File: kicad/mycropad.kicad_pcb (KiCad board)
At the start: 2 copper layers, 116.2 x 64.8 mm, 25 parts, among them SW1 SW_Push, SW2 SW_Push, SW3 SW_Push, SW4 SW_Push, SW5 SW_Push, SW6 SW_Push, SW7 SW_Push, SW8 SW_Push, U1 Pico, U2 SN74AHCT125N

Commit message: New reverse mount led. Let's hope it works...
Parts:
- added C1: 10uF, Capacitor_SMD:C_1206_3216Metric_Pad1.33x1.80mm_HandSolder, B.Cu at (116.8, 67.7)
- added C2: 10uF, Capacitor_SMD:C_1206_3216Metric_Pad1.33x1.80mm_HandSolder, B.Cu at (135.9, 67.7)
- added C3: 10uF, Capacitor_SMD:C_1206_3216Metric_Pad1.33x1.80mm_HandSolder, B.Cu at (116.8, 86.7)
- added C4: 10uF, Capacitor_SMD:C_1206_3216Metric_Pad1.33x1.80mm_HandSolder, B.Cu at (135.9, 86.7)
- added C5: 10uF, Capacitor_SMD:C_1206_3216Metric_Pad1.33x1.80mm_HandSolder, B.Cu at (116.8, 105.8)
- added C6: 10uF, Capacitor_SMD:C_1206_3216Metric_Pad1.33x1.80mm_HandSolder, B.Cu at (135.9, 105.8)
- added C7: 10uF, Capacitor_SMD:C_1206_3216Metric_Pad1.33x1.80mm_HandSolder, B.Cu at (154.9, 105.8)
- added C8: 10uF, Capacitor_SMD:C_1206_3216Metric_Pad1.33x1.80mm_HandSolder, B.Cu at (174.0, 105.8)
- D1, D2, D3, D4, D5, D6, D7, D8: value COM-12999 -> SK6812MINI-E; footprint LED_THT:LED_D5.0mm-4_RGB -> mycropad:LED_SK6812MINI-E_REV02_PLCC4_3.5x3.5mm_P1.75mm; moved to B.Cu
- moved D1 2.54 mm to (116.9, 70.9)
- moved D3 2.52 mm to (116.8, 89.9)
- moved D5 2.52 mm to (116.8, 109.0)
- moved D7 2.52 mm to (154.9, 109.0)
- moved D8 2.52 mm to (174.0, 109.0)
- moved D2 2.52 mm to (135.9, 70.9)
- moved D4 2.52 mm to (135.9, 89.9)
- moved D6 2.52 mm to (135.9, 109.0)
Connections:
- D1 pad 1: Net-(D1-Pad1) -> +5V
- D1 pad 2: +5V -> Net-(D1-Pad2)
- D2 pad 1: Net-(D1-Pad4) -> +5V
- D2 pad 2: +5V -> Net-(D2-Pad2)
- D2 pad 4: Net-(D2-Pad4) -> Net-(D1-Pad2)
- D3 pad 1: Net-(D2-Pad4) -> +5V
- D3 pad 2: +5V -> Net-(D3-Pad2)
- D3 pad 4: Net-(D3-Pad4) -> Net-(D2-Pad2)
- D4 pad 1: Net-(D3-Pad4) -> +5V
- D4 pad 2: +5V -> Net-(D4-Pad2)
- D4 pad 4: Net-(D4-Pad4) -> Net-(D3-Pad2)
- D5 pad 1: Net-(D4-Pad4) -> +5V
- D5 pad 2: +5V -> Net-(D5-Pad2)
- D5 pad 4: Net-(D5-Pad4) -> Net-(D4-Pad2)
- D6 pad 1: Net-(D5-Pad4) -> +5V
- D6 pad 2: +5V -> Net-(D6-Pad2)
- D6 pad 4: Net-(D6-Pad4) -> Net-(D5-Pad2)
- D7 pad 1: Net-(D6-Pad4) -> +5V
- D7 pad 2: +5V -> Net-(D7-Pad2)
- D7 pad 4: Net-(D7-Pad4) -> Net-(D6-Pad2)
- D8 pad 1: Net-(D7-Pad4) -> +5V
- D8 pad 2: +5V -> Net-(D8-Pad2)
- D8 pad 4: Net-(D8-Pad4) -> Net-(D7-Pad2)
- R1 pad 1: Net-(D1-Pad1) -> Net-(D1-Pad4)
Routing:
- net GND: track 418.7 -> 493.5 mm
- net Net-(D2-Pad2): track 0.00 -> 50.6 mm, vias 0 -> 2
- net Net-(D4-Pad2): track 0.00 -> 50.4 mm, vias 0 -> 2
- net Net-(D4-Pad4): track 42.5 -> 0.00 mm
- net Net-(D2-Pad4): track 42.5 -> 0.00 mm
- net Net-(D1-Pad1): track 39.8 -> 0.00 mm
- net Net-(D1-Pad4): track 15.2 -> 48.4 mm, vias 0 -> 1
- net +5V: track 227.2 -> 247.9 mm
- net Net-(D7-Pad4): track 15.2 -> 0.00 mm
- net Net-(D6-Pad4): track 15.2 -> 0.00 mm
- net Net-(D5-Pad4): track 15.2 -> 0.00 mm
- net Net-(D3-Pad4): track 15.2 -> 0.00 mm
- net Net-(D5-Pad2): track 0.00 -> 13.8 mm, vias 0 -> 2
- net Net-(D3-Pad2): track 0.00 -> 13.8 mm, vias 0 -> 2
- net Net-(D1-Pad2): track 0.00 -> 13.8 mm, vias 0 -> 2
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
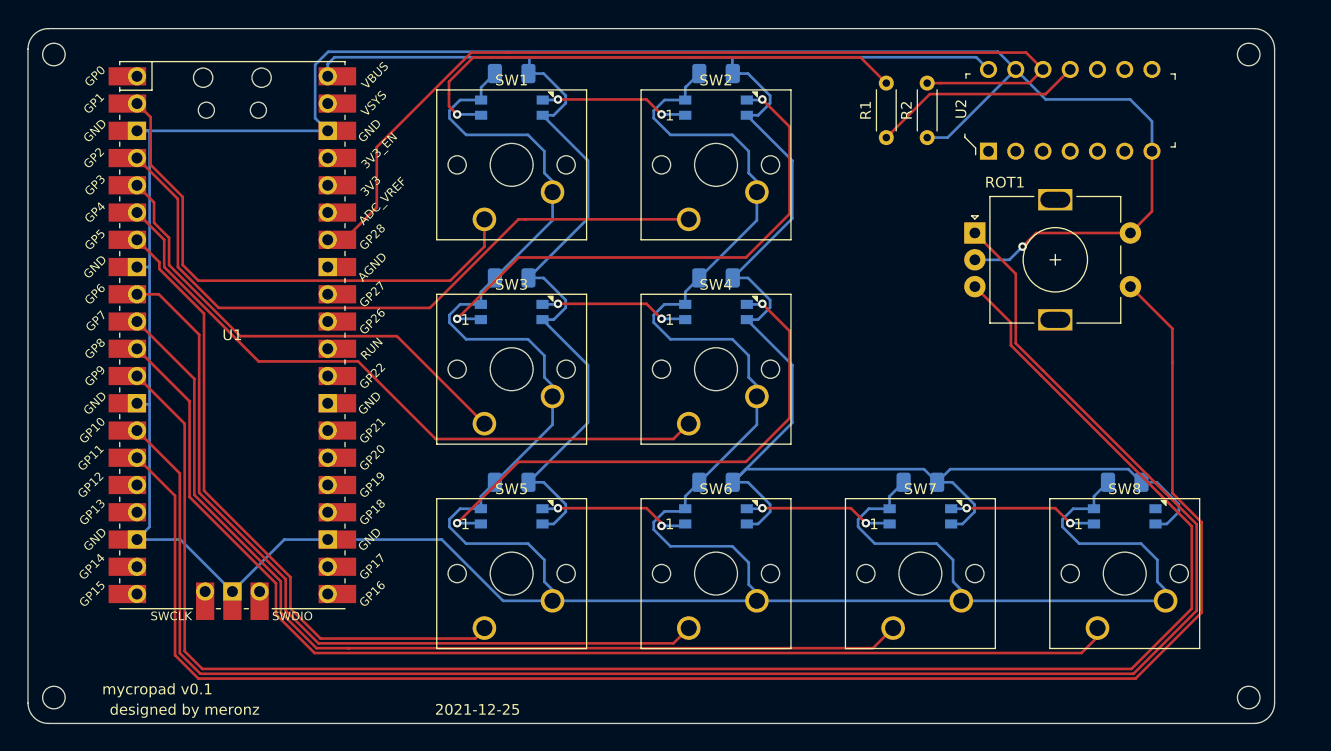
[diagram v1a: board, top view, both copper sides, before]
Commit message: Updated footprints for SK6812 MINI-E.
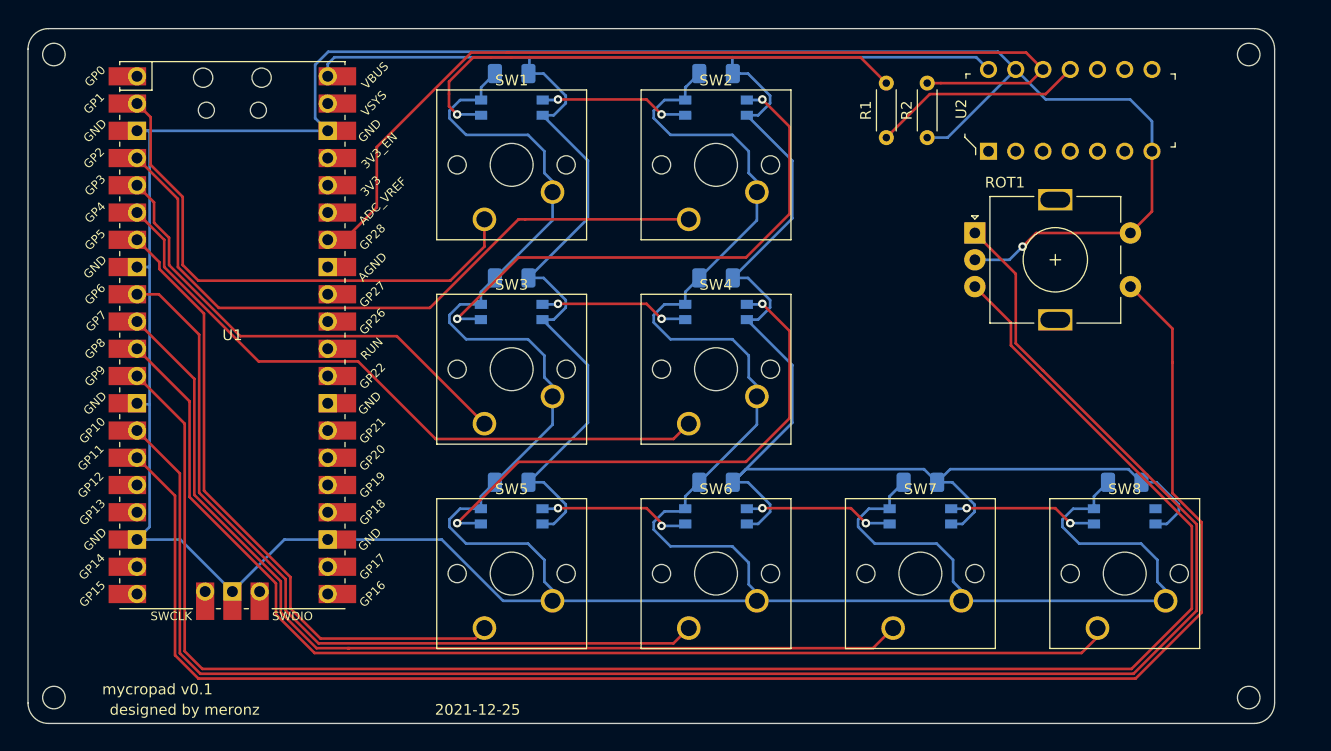
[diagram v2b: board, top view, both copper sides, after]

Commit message: mycropad v0.2 started.
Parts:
- D1, D2, D3, D4, D5, D6, D7, D8: footprint mycropad:LED_SK6812MINI-E_REV02_PLCC4_3.5x3.5mm_P1.75mm -> mycropad:LED_SK6812MINI-E_REV02_PLCC4_3.5x3.5mm_P1.75mm___V2
- moved U1 2.54 mm to (90.8, 89.5)
- moved REF** 0.38 mm to (185.2, 65.9)
- moved REF** 0.38 mm to (185.2, 125.9)
- moved REF** 0.06 mm to (74.2, 65.9)
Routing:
- net GPIO28: track 89.3 -> 78.6 mm
- net GND: track 493.5 -> 488.4 mm
- net GPIO5: track 60.0 -> 62.6 mm
- net GPIO11: track 152.1 -> 154.7 mm
- net GPIO9: track 162.9 -> 165.4 mm
- net GPIO6: track 75.8 -> 78.4 mm
- net GPIO10: track 164.2 -> 166.7 mm
- net GPIO1: track 49.4 -> 46.9 mm
- net GPIO8: track 109.7 -> 112.2 mm
- net GPIO7: track 92.1 -> 94.6 mm
- net GPIO3: track 44.2 -> 45.2 mm
- net GPIO2: track 64.4 -> 63.3 mm
- net GPIO4: track 62.3 -> 63.3 mm
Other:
- board size 116.2 x 64.8 mm -> 117 x 66 mm
- board text added: "mycropad v0.2"
- board text removed: "mycropad v0.1"

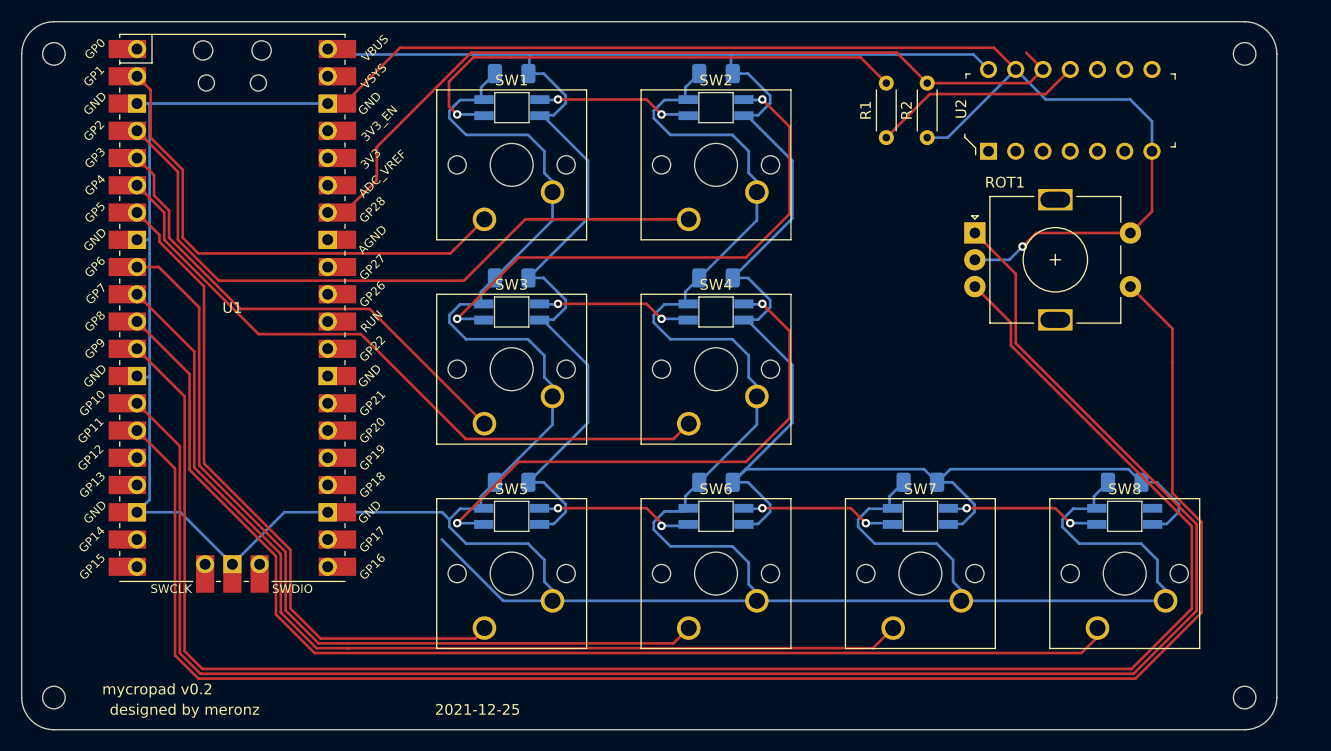
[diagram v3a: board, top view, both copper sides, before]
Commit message: Changed board layout, r1 & r2 footprints, added reset button
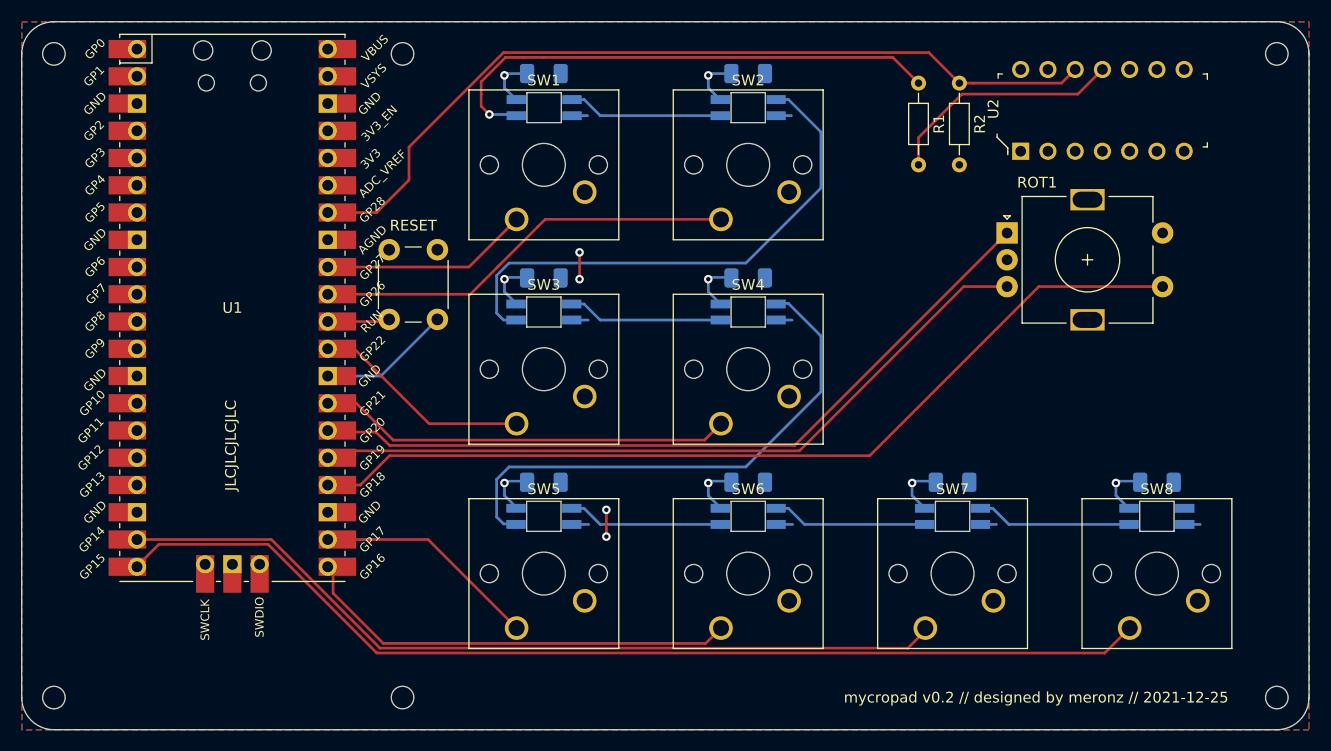
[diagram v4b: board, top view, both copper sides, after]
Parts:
- removed REF** (x2): MountingHole_2.1mm, MountingHole:MountingHole_2.1mm
- added M1: MountingHole_2.1mm, MountingHole:MountingHole_2.1mm, F.Cu at (74.2, 125.9)
- added M3: MountingHole_2.1mm, MountingHole:MountingHole_2.1mm, F.Cu at (106.7, 125.9)
- added M4: MountingHole_2.1mm, MountingHole:MountingHole_2.1mm, F.Cu at (106.7, 65.9)
- added M6: MountingHole_2.1mm, MountingHole:MountingHole_2.1mm, F.Cu at (188.2, 65.9)
- added SW9: RESET, Button_Switch_THT:SW_PUSH_6mm_H4.3mm, F.Cu at (105.4, 90.6)
- R1, R2: footprint Resistor_THT:R_Axial_DIN0204_L3.6mm_D1.6mm_P5.08mm_Horizontal -> Resistor_THT:R_Axial_DIN0204_L3.6mm_D1.6mm_P7.62mm_Horizontal
- moved C1 3.00 mm to (119.8, 67.7)
- moved C2 3.00 mm to (138.9, 67.7)
- moved C3 3.00 mm to (119.8, 86.7)
- moved C4 3.00 mm to (138.9, 86.7)
- moved C5 3.00 mm to (119.8, 105.8)
- moved C6 3.00 mm to (138.9, 105.8)
- moved C7 3.00 mm to (157.9, 105.8)
- moved C8 3.00 mm to (177.0, 105.8)
- moved D1 3.00 mm to (119.9, 70.9)
- moved D2 3.00 mm to (138.9, 70.9)
- moved D3 3.00 mm to (119.8, 89.9)
- moved D4 3.00 mm to (138.9, 89.9)
- moved D5 3.00 mm to (119.8, 109.0)
- moved D6 3.00 mm to (138.9, 109.0)
- moved D7 3.00 mm to (157.9, 109.0)
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- renumbered REF** to M2, REF** to M5
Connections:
- ROT1 pad A: GPIO10 -> ROT_DATA
- ROT1 pad B: GPIO9 -> ROT_CLK
- ROT1 pad S1: GPIO11 -> ROT_SW
- SW1 pad 1: GPIO1 -> SW1
- SW2 pad 1: GPIO2 -> SW2
- SW3 pad 1: GPIO3 -> SW3
- SW4 pad 1: GPIO4 -> SW4
- SW5 pad 1: GPIO5 -> SW5
- SW6 pad 1: GPIO6 -> SW6
- SW7 pad 1: GPIO7 -> SW7
- SW8 pad 1: GPIO8 -> SW8
- U1 pad 10: GPIO7 -> Net-(U1-Pad10)
- U1 pad 11: GPIO8 -> Net-(U1-Pad11)
- U1 pad 12: GPIO9 -> Net-(U1-Pad12)
- U1 pad 14: GPIO10 -> Net-(U1-Pad14)
- U1 pad 15: GPIO11 -> Net-(U1-Pad15)
- U1 pad 18: GND -> Net-(U1-Pad18)
- U1 pad 19: Net-(U1-Pad19) -> SW7
- U1 pad 2: GPIO1 -> Net-(U1-Pad2)
- U1 pad 20: Net-(U1-Pad20) -> SW8
- U1 pad 21: Net-(U1-Pad21) -> SW6
- U1 pad 22: Net-(U1-Pad22) -> SW5
- U1 pad 23: GND -> Net-(U1-Pad23)
- U1 pad 24: Net-(U1-Pad24) -> ROT_SW
- U1 pad 25: Net-(U1-Pad25) -> ROT_CLK
- U1 pad 26: Net-(U1-Pad26) -> ROT_DATA
- U1 pad 27: Net-(U1-Pad27) -> SW4
- U1 pad 28: Net-(U1-Pad28) -> GND
- U1 pad 29: Net-(U1-Pad29) -> SW3
- U1 pad 3: GND -> Net-(U1-Pad3)
- U1 pad 30: Net-(U1-Pad30) -> RUN
- U1 pad 31: Net-(U1-Pad31) -> SW2
- U1 pad 32: Net-(U1-Pad32) -> SW1
- U1 pad 4: GPIO2 -> Net-(U1-Pad4)
- U1 pad 42: GND -> Net-(U1-Pad42)
- U1 pad 5: GPIO3 -> Net-(U1-Pad5)
- U1 pad 6: GPIO4 -> Net-(U1-Pad6)
- U1 pad 7: GPIO5 -> Net-(U1-Pad7)
- U1 pad 8: GND -> Net-(U1-Pad8)
- U1 pad 9: GPIO6 -> Net-(U1-Pad9)
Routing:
- net GND: track 488.4 -> 49.4 mm, vias 1 -> 8
- net +5V: track 247.5 -> 17.0 mm, vias 0 -> 4
- net GPIO10: track 166.7 -> 0.00 mm
- net GPIO9: track 165.4 -> 0.00 mm
- net GPIO11: track 154.7 -> 0.00 mm
- net GPIO8: track 112.2 -> 0.00 mm
- net SW8: track 0.00 -> 98.6 mm
- net GPIO7: track 94.6 -> 0.00 mm
- net ROT_SW: track 0.00 -> 85.5 mm
- net GPIO6: track 78.4 -> 0.00 mm
- net SW7: track 0.00 -> 78.1 mm
- net ROT_DATA: track 0.00 -> 71.6 mm
- net ROT_CLK: track 0.00 -> 69.4 mm
- net GPIO4: track 63.3 -> 0.00 mm
- net GPIO2: track 63.3 -> 0.00 mm
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- added copper zone on B.Cu, net +5V
- added copper zone on F.Cu, net GND
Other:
- board size 117 x 66 mm -> 120 x 66 mm
- board text added: "JLCJLCJLCJLC"
- board text added: "mycropad v0.2 // designed by meronz // 2021-12-25"
- board text removed: "2021-12-25"
- board text removed: "designed by meronz"
- board text removed: "mycropad v0.2"

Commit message: v0.2 enclosure, with new cover and inclined base
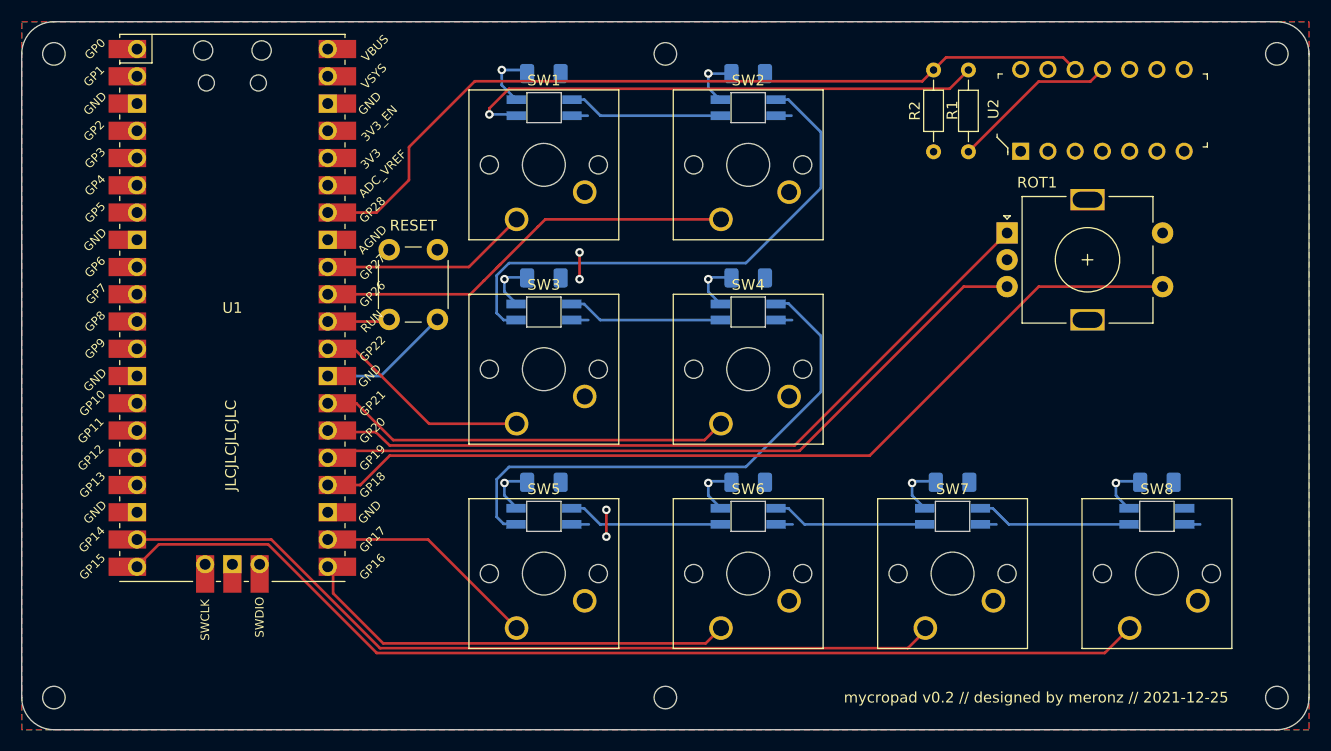
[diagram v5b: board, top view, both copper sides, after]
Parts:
- moved M3 24.5 mm to (131.2, 125.9)
- moved M4 24.5 mm to (131.2, 65.9)
- moved R1 4.81 mm to (159.4, 67.4)
- moved R2 2.70 mm to (156.2, 67.4)
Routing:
- net NEOPIX_5v: track 22.3 -> 15.7 mm
- net GPIO28: track 78.9 -> 77.4 mm
- net GND: track 49.4 -> 50.5 mm
- net Net-(D1-Pad4): track 48.4 -> 49.1 mm

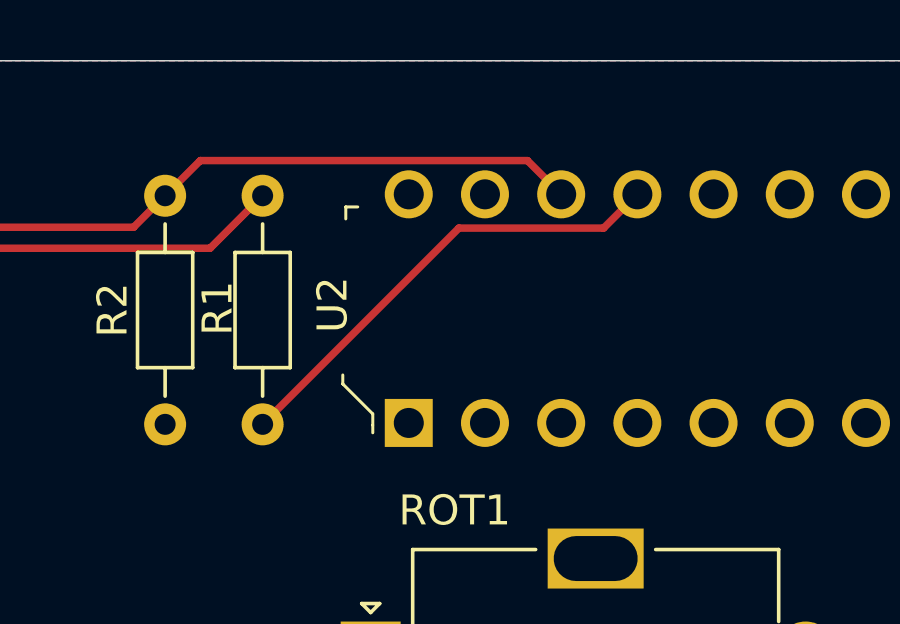
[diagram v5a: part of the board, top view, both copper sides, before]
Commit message: New pcb holes layout
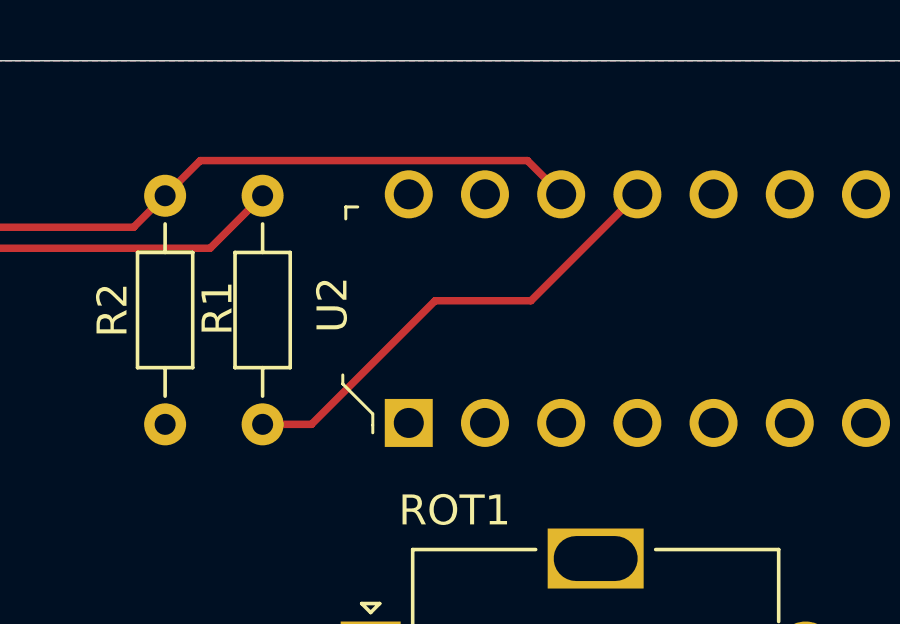
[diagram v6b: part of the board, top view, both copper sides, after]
